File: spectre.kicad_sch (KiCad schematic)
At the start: 0 parts

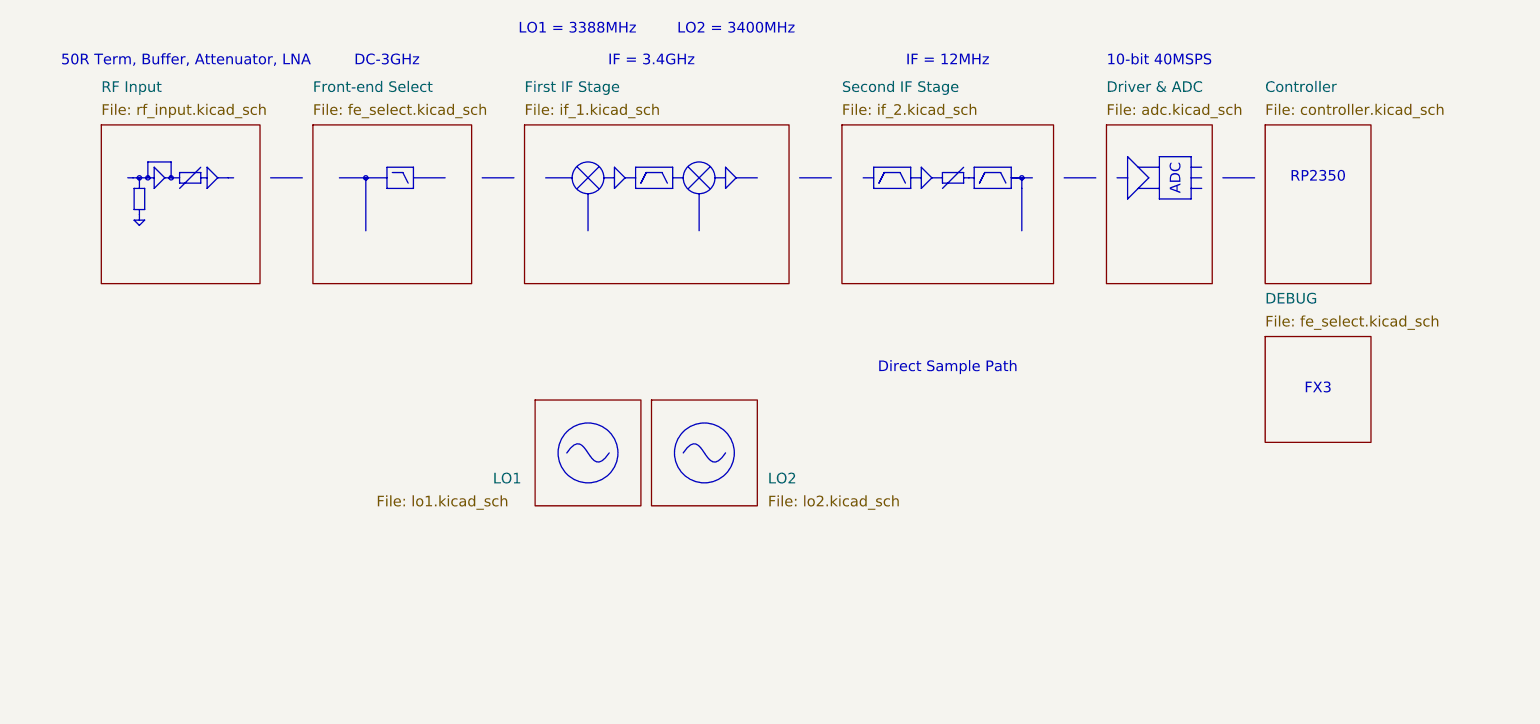
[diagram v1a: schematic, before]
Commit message: added labels to LO, duplicated to LO2
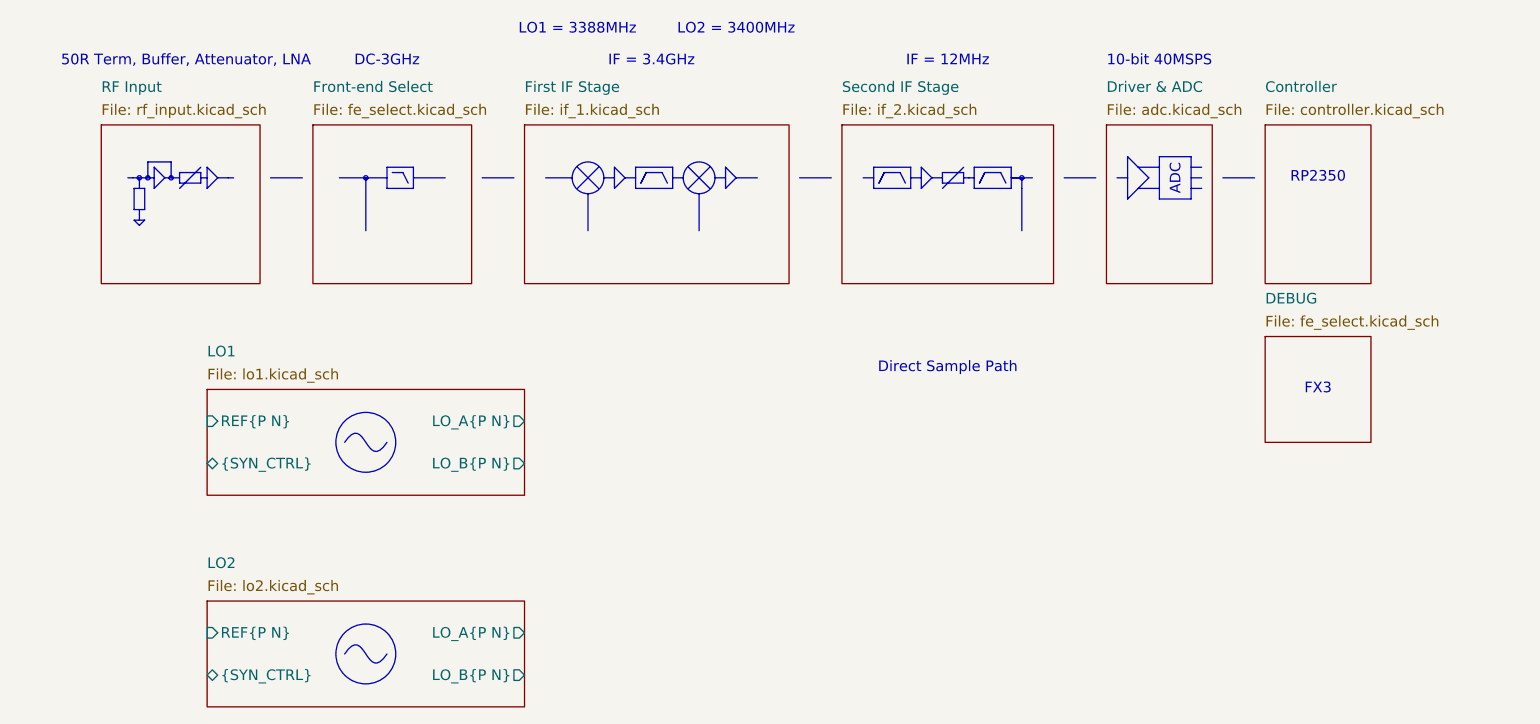
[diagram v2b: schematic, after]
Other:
- sheet LO1 ports: added LO_A{P N}, LO_B{P N}, REF{P N}, {SYN_CTRL}; removed none
- sheet LO2 ports: added LO_A{P N}, LO_B{P N}, REF{P N}, {SYN_CTRL}; removed none
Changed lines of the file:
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@@
 	(bezier
 		(pts
-			(xy 93.98 96.52) (xy 96.52 92.71) (xy 96.52 100.33) (xy 99.06 96.52)
+			(xy 67.31 95.25) (xy 69.85 91.44) (xy 69.85 99.06) (xy 72.39 95.25)
 		)
 		(stroke
@@
 	)
 	(circle
-		(center 110.49 96.52)
+		(center 69.85 120.65)
 		(radius 3.5921)
 		(stroke
@@
 	(bezier
 		(pts
-			(xy 107.95 96.52) (xy 110.49 92.71) (xy 110.49 100.33) (xy 113.03 96.52)
+			(xy 67.31 120.65) (xy 69.85 116.84) (xy 69.85 124.46) (xy 72.39 120.65)
 		)
 		(stroke
@@
 	)
 	(circle
-		(center 96.52 96.52)
+		(center 69.85 95.25)
 		(radius 3.5921)
 		(stroke
@@
 	)
 	(sheet
-		(at 104.14 90.17)
-		(size 12.7 12.7)
-		(exclude_from_sim no)
-		(in_bom yes)
-		(on_board yes)
-		(dnp no)
-		(stroke
-			(width 0.1524)
-			(type solid)
-		)
-		(fill
-			(color 0 0 0 0)
-		)
-		(property "Sheetname" "LO2"
-			(at 118.11 100.33 0)
-			(show_name no)
-			(do_not_autoplace no)
-			(effects
-				(font
-					(size 1.27 1.27)
-				)
-				(justify left bottom)
-			)
-		)
-		(property "Sheetfile" "lo2.kicad_sch"
-			(at 118.11 101.6 0)
-			(show_name no)
-			(do_not_autoplace no)
-			(effects
-				(font
-					(size 1.27 1.27)
-				)
-				(justify left top)
-			)
-		)
-		(instances
-			(project "spectre"
-				(path "/e2b3a745-ca2b-407e-8017-842114c52164"
-					(page "11")
-				)
-			)
-		)
-	)
-	(sheet
 		(at 127 57.15)
 		(size 25.4 19.05)
@@
 	)
 	(sheet
-		(at 90.17 90.17)
-		(size 12.7 12.7)
+		(at 50.8 88.9)
+		(size 38.1 12.7)
 		(exclude_from_sim no)
 		(in_bom yes)
@@
 		)
 		(property "Sheetname" "LO1"
-			(at 85.09 100.33 0)
+			(at 50.8 85.09 0)
 			(show_name no)
 			(do_not_autoplace no)
@@
 		)
 		(property "Sheetfile" "lo1.kicad_sch"
-			(at 71.12 101.6 0)
+			(at 50.8 86.36 0)
 			(show_name no)
 			(do_not_autoplace no)
@@
 				)
 				(justify left top)
+			)
+		)
+		(pin "LO_A{P N}" output
+			(at 88.9 92.71 0)
+			(effects
+				(font
+					(size 1.27 1.27)
+				)
+				(justify right)
+			)
+		)
+		(pin "LO_B{P N}" output
+			(at 88.9 97.79 0)
+			(effects
+				(font
+					(size 1.27 1.27)
+				)
+				(justify right)
+			)
+		)
+		(pin "REF{P N}" input
+			(at 50.8 92.71 180)
+			(effects
+				(font
+					(size 1.27 1.27)
+				)
+				(justify left)
+			)
+		)
+		(pin "{SYN_CTRL}" bidirectional
+			(at 50.8 97.79 180)
+			(effects
+				(font
+					(size 1.27 1.27)
+				)
+				(justify left)
 			)
 		)
@@
 				)
 			)
+		)
+	)
+	(sheet
+		(at 50.8 114.3)
+		(size 38.1 12.7)
+		(exclude_from_sim no)
+		(in_bom yes)
+		(on_board yes)
+		(dnp no)
+		(stroke
+			(width 0.1524)
+			(type solid)
+		)
+		(fill
+			(color 0 0 0 0)
+		)
+		(property "Sheetname" "LO2"
+			(at 50.8 110.49 0)
+			(show_name no)
+			(do_not_autoplace no)
+			(effects
+				(font
+					(size 1.27 1.27)
+				)
+				(justify left bottom)
+			)
+		)
+		(property "Sheetfile" "lo2.kicad_sch"
+			(at 50.8 111.76 0)
+			(show_name no)
+			(do_not_autoplace no)
+			(effects
+				(font
+					(size 1.27 1.27)
+				)
+				(justify left top)
+			)
+		)
+		(pin "LO_A{P N}" output
+			(at 88.9 118.11 0)
+			(effects
+				(font
+					(size 1.27 1.27)
+				)
+				(justify right)
+			)
+		)
+		(pin "LO_B{P N}" output
+			(at 88.9 123.19 0)
+			(effects
+				(font
+					(size 1.27 1.27)
+				)
+				(justify right)
+			)
+		)
+		(pin "REF{P N}" input
+			(at 50.8 118.11 180)
+			(effects
+				(font
+					(size 1.27 1.27)
+				)
+				(justify left)
+			)
+		)
+		(pin "{SYN_CTRL}" bidirectional
+			(at 50.8 123.19 180)
+			(effects
+				(font
+					(size 1.27 1.27)
+				)
+				(justify left)
+			)
+		)
+		(instances
+			(project "spectre"
+				(path "/e2b3a745-ca2b-407e-8017-842114c52164"
+					(page "10")
+				)
+			)

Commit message: used instanced sheet for LO, design block, synth placement
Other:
- sheet LO1: file lo1.kicad_sch -> lo.kicad_sch
- sheet LO2: file lo2.kicad_sch -> lo.kicad_sch
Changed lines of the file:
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@@
 			)
 		)
-		(property "Sheetfile" "lo1.kicad_sch"
+		(property "Sheetfile" "lo.kicad_sch"
 			(at 50.8 86.36 0)
 			(show_name no)
@@
 			)
 		)
-		(property "Sheetfile" "lo2.kicad_sch"
+		(property "Sheetfile" "lo.kicad_sch"
 			(at 50.8 111.76 0)
 			(show_name no)
